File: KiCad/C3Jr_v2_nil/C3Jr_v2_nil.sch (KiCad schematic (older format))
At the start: 68 parts, among them IC1 ATTINY85-P, P1 PWM_0, P2 PWM_1, P3 A_IN, P4 ISP, P5 STACK-L, P6 STACK-R, P7 DC_IN_1, P8 DC_IN_2, Q1 PNP, Q2 PNP, X1 CRYSTAL

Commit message: C3Jr_v2_nil - Name in Lights for C3Jr - to light up custom names on face plates
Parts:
- added C3, C4, C5: 100n, symbol C
- C1, C2: value C -> 22p
- renumbered IC1 to U1
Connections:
- wire segments 202 -> 166
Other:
- moved on the sheet: P8

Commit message: C3Jr_v2_nil : Name in Lights, initial board layout.
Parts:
- removed D17, D18, D19, D20, D21, D22, D23, D24, D25, D26, D27, D28, D29, D30, D31, D32: LED, symbol LED
- removed P1: PWM_0, symbol CONN_2
- removed P2: PWM_1, symbol CONN_2
- removed Q2: PNP, symbol PNP
- removed R10: 1k, symbol R
- removed R11, R12, R13, R14, R15, R16, R17, R18: 47E, symbol R
- removed R20: 10k, symbol R
- removed R22: LDR2, symbol R
- removed X1: CRYSTAL, symbol CRYSTAL
- added CD2: CDOT2, symbol CONN_4
- added K1: CONN_3, symbol CONN_3
- added P10, P11, P14, P15, P9, rowBoB1: CONN_1, symbol CONN_1
- added P24, P25, P26, P27, P28, P29, P30, P31, P32, P33, P34, P35, P36, P37, P38, P39: DIL6, PROTO-6, symbol DIL6
- added SP1: SPEAKER, symbol CONN_2
- added X1: CRYSTAL2, symbol CRYSTAL2
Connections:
- net labels removed: MISO_PWM_1
- wire segments 166 -> 256
- no-connect marks 0 -> 6
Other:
- note added: "Mounting Holes"
- note added: "PROTO AREA"
- note added: "allows same board to be used\nat different locations by selecting\none of two PWM pins"
- note removed: "Enable/Disable\njumpers, if reqd.\nduring programming"
- note removed: "LOWER bank of LEDs"
- moved on the sheet: R1

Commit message: C3Jr_v2_nil - revised PCB , smaller size
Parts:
- removed P11, P14, P15, rowBoB1: CONN_1, symbol CONN_1
- removed P24, P25, P26, P27, P28, P29, P30, P31, P32, P33, P34, P35: DIL6, PROTO-6, symbol DIL6
- removed P5: STACK-L, symbol CONN_4
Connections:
- wire segments 256 -> 160
- no-connect marks 6 -> 2

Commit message: C3Jr_v2_nil - revised PCB , smaller size, removed ATTiny and other parts
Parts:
- removed C1, C2: 22p, symbol C
- removed C3, C4: 100n, symbol C
- removed CD2: CDOT2, symbol CONN_4
- removed P3: A_IN, symbol CONN_4
- removed P39: DIL6, PROTO-6, symbol DIL6
- removed P4: ISP, symbol CONN_6
- removed P6: STACK-R, symbol CONN_4
- removed P8: DC_IN_2, symbol CONN_2
- removed R19: 10k, symbol R
- removed R21: LDR1, symbol R
- removed U1: ATTINY85-P, DIP8, symbol ATTINY85-P
- removed X1: CRYSTAL2, symbol CRYSTAL2
- added P3, P4: CONN_1, symbol CONN_1
- P6: renamed from K1; value CONN_3 -> DC_IN_2
- Q1: value PNP -> PBSS9110Z
- renumbered P9 to P1, P10 to P2, P7 to P5, P36 to P7, P37 to P8, P38 to P9, R2 to R1, R3 to R2, R4 to R3, R5 to R4, R6 to R5, R7 to R6, R8 to R7, R9 to R8, R1 to R9
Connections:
- net labels removed: MISO_PWM1, MOSI_PWM0_SDA, PB3_ADC3, PB4_ADC2, RST, SCK_SCL
- wire segments 160 -> 83
- no-connect marks 2 -> 4
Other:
- note removed: "allows same board to be used\nat different locations by selecting\none of two PWM pins"
- note removed: "these are also used to\nmount the lower board\nto C3Jr @ Stack-LR"
- note removed: "to connect external\nanalog IN like LDR"
- moved on the sheet: C5, D1, D10, D11, D12, D13, D14, D15, D16, D2, D3, D4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

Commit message: C3Jr_v2_nil - work in progress on NiL board
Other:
- note added: "C3Jr-Name-in-Lights\n------------------------\nan array of 16 SMD LEDs driven either via Speaker Transistor on C3Jr\nusing SP1 for control signal and P5/P6 for Power (+5V, GND)\nOR, by using on board Transistor with Base Resistor, via any other\navailable control pin on the controller.\nIf using on-board Transistor, Pin 3 of connector P6 gets terminated\non Proto Area, and can be red-wired to app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"
- note removed: "UPPER bank of LEDs"
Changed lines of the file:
@@
-EESchema Schematic File Version 2  date 5/4/2012 5:25:38 PM
+EESchema Schematic File Version 2  date 5/5/2012 12:21:39 PM
 LIBS:C3Jr_v2_nil
 LIBS:ATtiny85_bmp
@@
 Sheet 1 1
 Title ""
-Date "4 may 2012"
+Date "5 may 2012"
 Rev ""
 Comp ""
@@
 Comment4 ""
 $EndDescr
+Text Notes 7050 6300 0    60   ~ 12
+C3Jr-Name-in-Lights\n------------------------\nan array of 16 SMD LEDs driven either via Speaker Transistor on C3Jr\nusing SP1 for control signal and P5/P6 for Power (+5V, GND)\nOR, by using on board Transistor with Base Resistor, via any other\navailable control pin on the controller.\nIf using on-board Transistor, Pin 3 of connector P6 gets terminated\non Proto Area, and can be red-wired to appropriate control pin.
 $Comp
 L CONN_1 P3
@@
 	1    0    0    -1
 $EndComp
-Text Notes 7250 3700 0    40   ~ 0
-UPPER bank of LEDs
 Text Notes 1350 3300 0    40   ~ 0
 these are also used to\nmount the Upper board\nto C3Jr @ Proto area

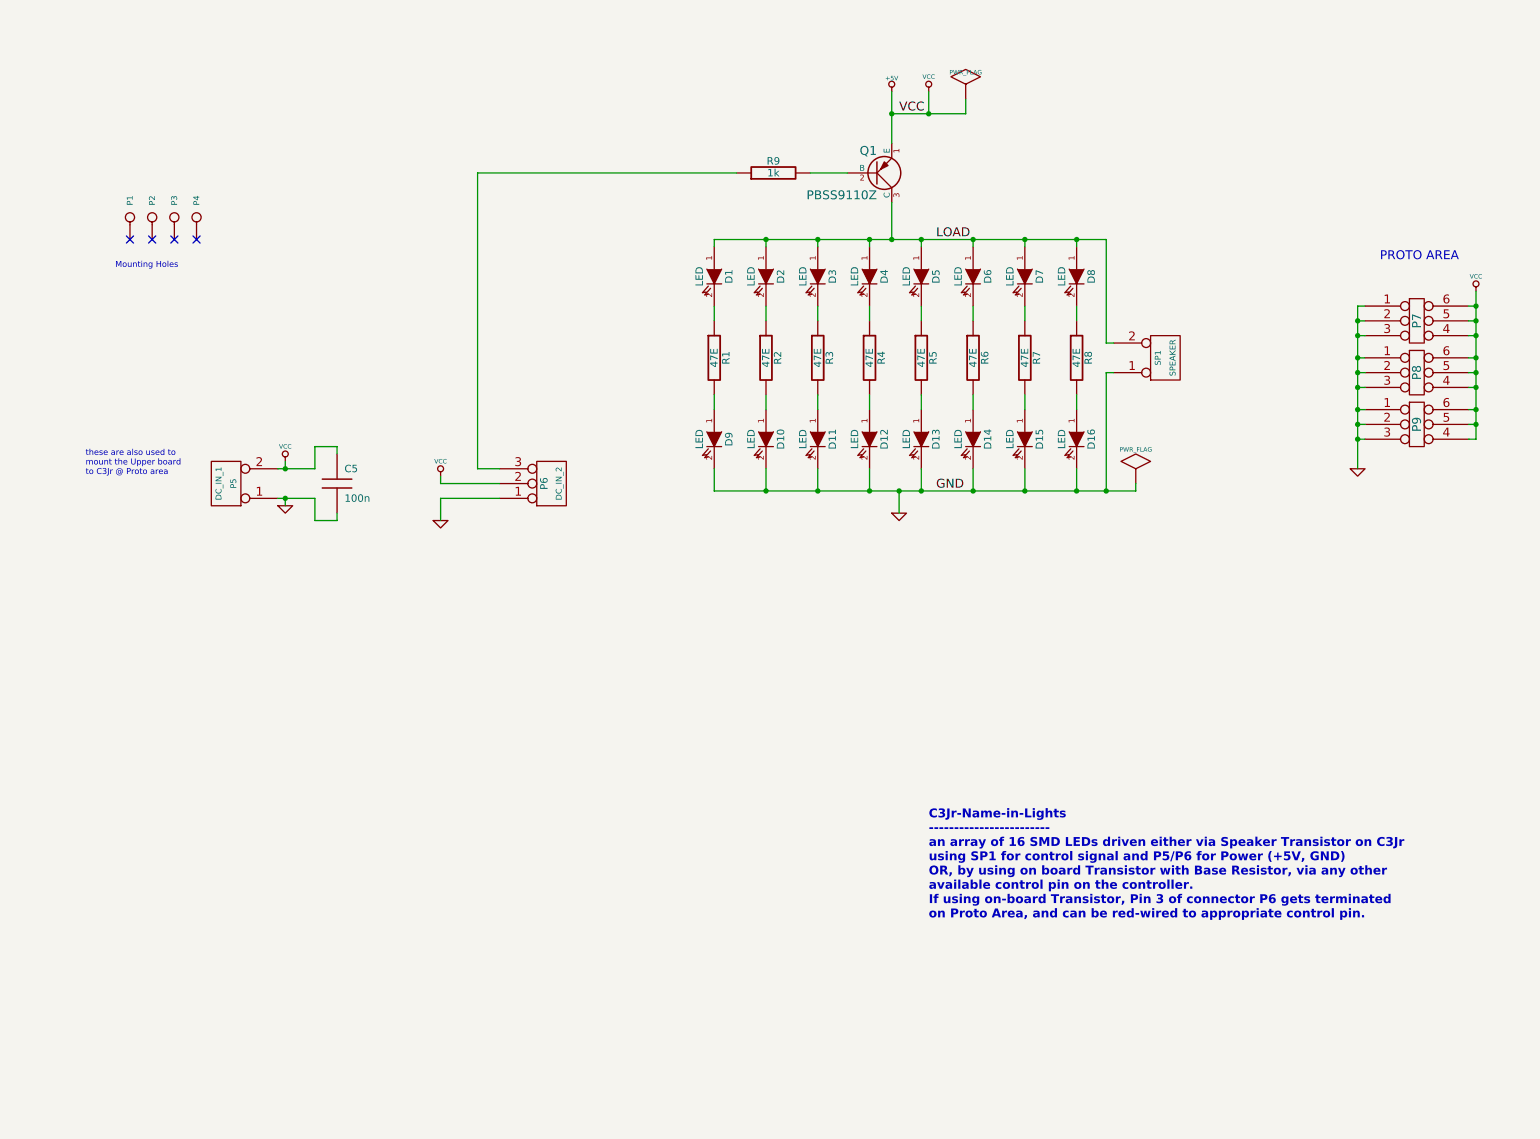
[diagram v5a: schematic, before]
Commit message: C3Jr_v2_nil : almost complete. Final checks required. Test circuit.
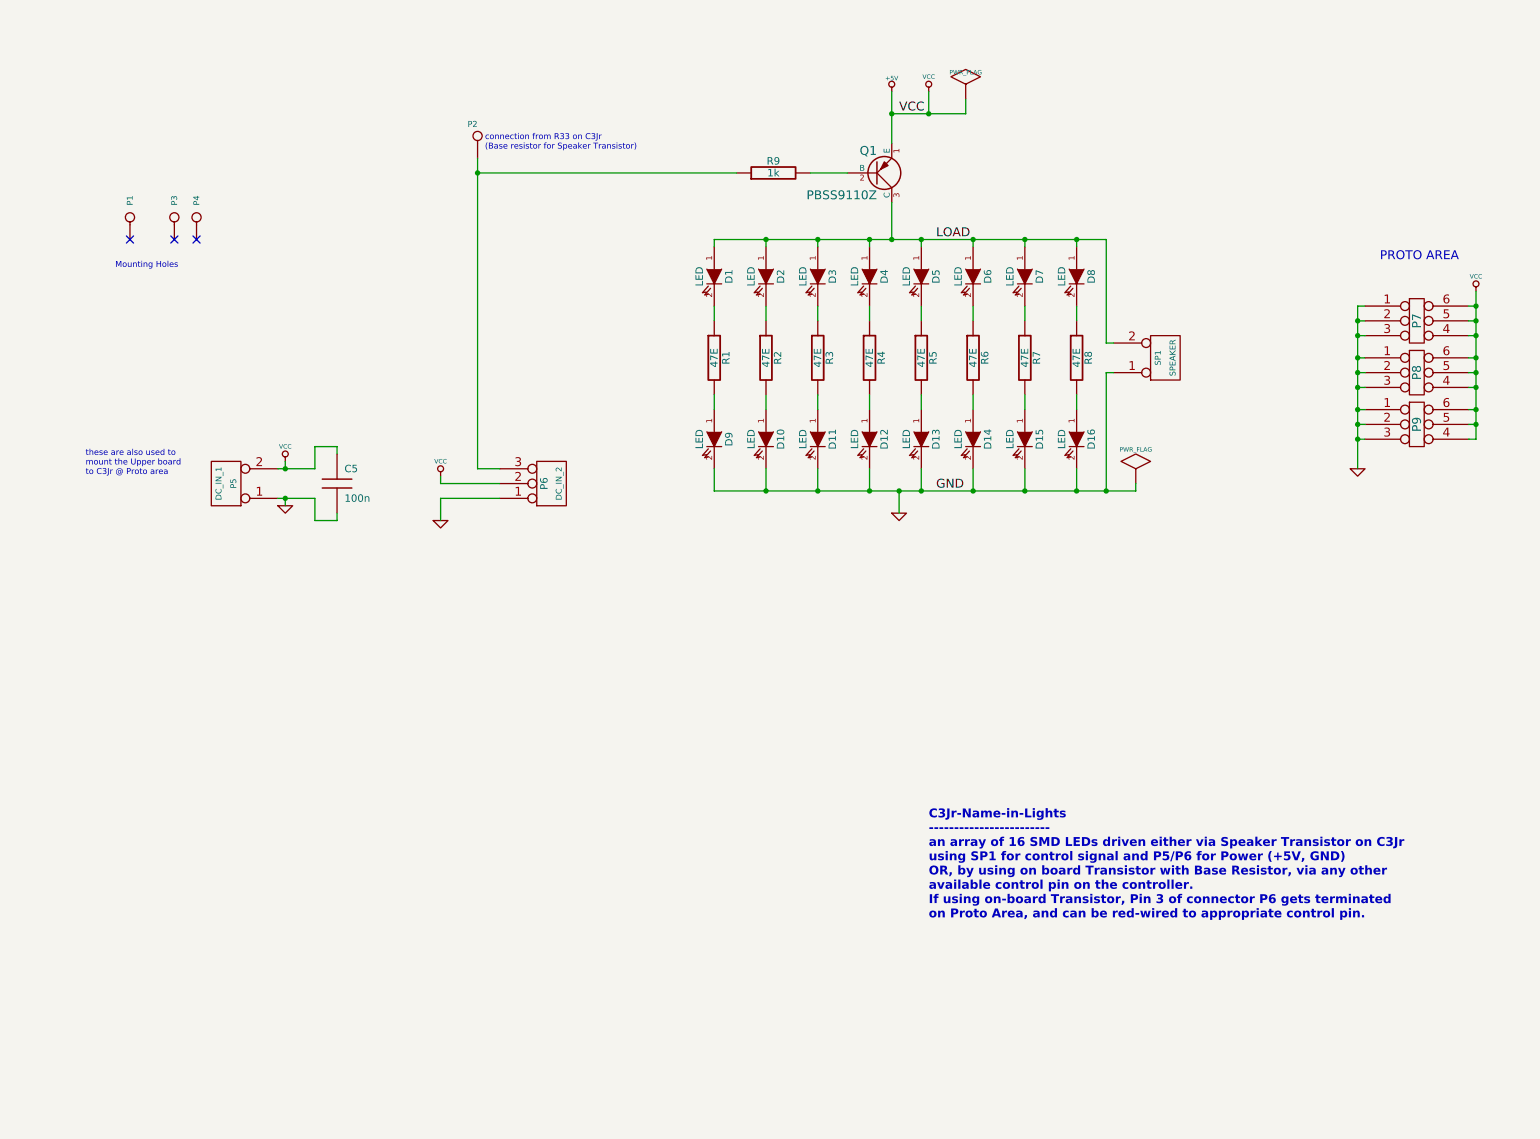
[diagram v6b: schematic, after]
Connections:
- net at P6.3 (P3), R9.1: now also P2.1
- no-connect marks 4 -> 3
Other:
- note added: "connection from R33 on C3Jr\n(Base resistor for Speaker Transistor)"
- moved on the sheet: P2
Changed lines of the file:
@@
-EESchema Schematic File Version 2  date 5/5/2012 12:21:39 PM
+EESchema Schematic File Version 2  date Sunday 06 May 2012 12:23:57 AM IST
 LIBS:C3Jr_v2_nil
 LIBS:ATtiny85_bmp
@@
 Comment4 ""
 $EndDescr
+Text Notes 4050 1100 0    40   ~ 0
+connection from R33 on C3Jr\n(Base resistor for Speaker Transistor)
+Connection ~ 4000 1250
+Wire Wire Line
+	4000 1150 4000 3250
+Wire Wire Line
+	9950 3250 9950 2150
+Connection ~ 8050 1700
+Wire Wire Line
+	8250 1700 5600 1700
+Wire Wire Line
+	8250 1700 8250 2400
+Wire Wire Line
+	8250 2400 8300 2400
+Connection ~ 2700 3450
+Wire Wire Line
+	2650 3450 2900 3450
+Wire Wire Line
+	2900 3450 2900 3600
+Wire Wire Line
+	2900 3600 3050 3600
+Wire Wire Line
+	3050 3600 3050 3550
+Wire Wire Line
+	4150 3350 3750 3350
+Wire Wire Line
+	3750 3350 3750 3300
+Wire Wire Line
+	2700 3500 2700 3450
+Wire Wire Line
+	2700 3200 2700 3250
+Wire Wire Line
+	7700 2150 7700 2250
+Wire Wire Line
+	7000 2150 7000 2250
+Wire Wire Line
+	6300 2150 6300 2250
+Wire Wire Line
+	5600 2150 5600 2250
+Connection ~ 6850 3400
+Wire Wire Line
+	6850 3400 6850 3550
+Wire Wire Line
+	6250 1250 6500 1250
+Wire Wire Line
+	6800 1050 6800 700
+Wire Wire Line
+	7700 1700 7700 1750
+Wire Wire Line
+	7000 1700 7000 1750
+Wire Wire Line
+	6300 1700 6300 1750
+Wire Wire Line
+	5600 1700 5600 1750
+Wire Wire Line
+	7700 2750 7700 2850
+Wire Wire Line
+	7000 2750 7000 2850
+Wire Wire Line
+	6300 2750 6300 2850
+Wire Wire Line
+	5600 2750 5600 2850
+Connection ~ 7350 3400
+Wire Wire Line
+	7350 3400 7350 3250
+Connection ~ 6650 3400
+Wire Wire Line
+	6650 3400 6650 3250
+Connection ~ 5950 3400
+Wire Wire Line
+	5950 3400 5950 3250
+Connection ~ 7350 1700
+Connection ~ 6650 1700
+Connection ~ 5950 1700
+Wire Wire Line
+	8050 3250 8050 3400
+Wire Wire Line
+	5600 3250 5600 3400
+Connection ~ 6300 1700
+Connection ~ 7000 1700
+Connection ~ 7700 1700
+Wire Wire Line
+	6300 3400 6300 3250
+Connection ~ 6300 3400
+Wire Wire Line
+	7000 3400 7000 3250
+Connection ~ 7000 3400
+Wire Wire Line
+	7700 3400 7700 3250
+Connection ~ 7700 3400
+Wire Wire Line
+	5950 2750 5950 2850
+Wire Wire Line
+	6650 2750 6650 2850
+Wire Wire Line
+	7350 2750 7350 2850
+Wire Wire Line
+	8050 2750 8050 2850
+Wire Wire Line
+	5950 1750 5950 1700
+Wire Wire Line
+	6650 1700 6650 1750
+Wire Wire Line
+	7350 1700 7350 1750
+Wire Wire Line
+	8050 1700 8050 1750
+Wire Wire Line
+	6800 1700 6800 1450
+Connection ~ 6800 1700
+Wire Wire Line
+	7050 700  7050 850
+Connection ~ 6800 850
+Wire Wire Line
+	7300 750  7300 850
+Wire Wire Line
+	7300 850  6800 850
+Connection ~ 7050 850
+Wire Wire Line
+	5950 2150 5950 2250
+Wire Wire Line
+	6650 2150 6650 2250
+Wire Wire Line
+	7350 2150 7350 2250
+Wire Wire Line
+	8050 2150 8050 2250
+Wire Wire Line
+	3750 3600 3750 3450
+Wire Wire Line
+	3750 3450 4150 3450
+Wire Wire Line
+	3050 3150 3050 3100
+Wire Wire Line
+	3050 3100 2900 3100
+Wire Wire Line
+	2900 3100 2900 3250
+Wire Wire Line
+	2900 3250 2650 3250
+Connection ~ 2700 3250
+Connection ~ 10750 2150
+Wire Wire Line
+	10750 2050 10750 3050
+Wire Wire Line
+	10750 3050 10700 3050
+Connection ~ 10750 2850
+Wire Wire Line
+	10750 2850 10700 2850
+Connection ~ 10750 2600
+Wire Wire Line
+	10750 2600 10700 2600
+Connection ~ 10750 2350
+Wire Wire Line
+	10750 2350 10700 2350
+Connection ~ 9950 2250
+Wire Wire Line
+	10000 2250 9950 2250
+Connection ~ 9950 2500
+Wire Wire Line
+	9950 2500 10000 2500
+Connection ~ 9950 2700
+Wire Wire Line
+	9950 2700 10000 2700
+Connection ~ 9950 2950
+Wire Wire Line
+	9950 2950 10000 2950
+Wire Wire Line
+	10750 2150 10700 2150
+Wire Wire Line
+	9950 2150 10000 2150
+Wire Wire Line
+	9950 3050 10000 3050
+Connection ~ 9950 3050
+Wire Wire Line
+	9950 2850 10000 2850
+Connection ~ 9950 2850
+Wire Wire Line
+	9950 2600 10000 2600
+Connection ~ 9950 2600
+Wire Wire Line
+	9950 2350 10000 2350
+Connection ~ 9950 2350
+Wire Wire Line
+	10750 2250 10700 2250
+Connection ~ 10750 2250
+Wire Wire Line
+	10750 2500 10700 2500
+Connection ~ 10750 2500
+Wire Wire Line
+	10750 2700 10700 2700
+Connection ~ 10750 2700
+Wire Wire Line
+	10750 2950 10700 2950
+Connection ~ 10750 2950
+Wire Wire Line
+	8300 2600 8250 2600
+Wire Wire Line
+	8250 2600 8250 3400
+Connection ~ 8050 3400
+Wire Wire Line
+	4000 1250 5750 1250
+Wire Wire Line
+	4000 3250 4150 3250
+Wire Wire Line
+	8450 3350 8450 3400
+Wire Wire Line
+	8450 3400 5600 3400
+Connection ~ 8250 3400
 Text Notes 7050 6300 0    60   ~ 12
 C3Jr-Name-in-Lights\n------------------------\nan array of 16 SMD LEDs driven either via Speaker Transistor on C3Jr\nusing SP1 for control signal and P5/P6 for Power (+5V, GND)\nOR, by using on board Transistor with Base Resistor, via any other\navailable control pin on the controller.\nIf using on-board Transistor, Pin 3 of connector P6 gets terminated\non Proto Area, and can be red-wired to appropriate control pin.
@@
 $EndComp
 NoConn ~ 2100 1700
-Connection ~ 8250 3400
-Wire Wire Line
-	8450 3400 5600 3400
-Wire Wire Line
-	8450 3400 8450 3350
-Wire Wire Line
-	4150 3250 4000 3250
-Wire Wire Line
-	4000 3250 4000 1250
-Wire Wire Line
-	4000 1250 5750 1250
-Connection ~ 8050 3400
-Wire Wire Line
-	8250 3400 8250 2600
-Wire Wire Line
-	8250 2600 8300 2600
-Connection ~ 10750 2950
-Wire Wire Line
-	10750 2950 10700 2950
-Connection ~ 10750 2700
-Wire Wire Line
-	10750 2700 10700 2700
-Connection ~ 10750 2500
-Wire Wire Line
-	10750 2500 10700 2500
-Connection ~ 10750 2250
-Wire Wire Line
-	10750 2250 10700 2250
-Connection ~ 9950 2350
-Wire Wire Line
-	9950 2350 10000 2350
-Connection ~ 9950 2600
-Wire Wire Line
-	9950 2600 10000 2600
-Connection ~ 9950 2850
-Wire Wire Line
-	9950 2850 10000 2850
-Connection ~ 9950 3050
-Wire Wire Line
-	9950 3050 10000 3050
-Wire Wire Line
-	10000 2150 9950 2150
-Wire Wire Line
-	10750 2150 10700 2150
-Wire Wire Line
-	9950 2950 10000 2950
-Connection ~ 9950 2950
-Wire Wire Line
-	9950 2700 10000 2700
-Connection ~ 9950 2700
-Wire Wire Line
-	9950 2500 10000 2500
-Connection ~ 9950 2500
-Wire Wire Line
-	10000 2250 9950 2250
-Connection ~ 9950 2250
-Wire Wire Line
-	10750 2350 10700 2350
-Connection ~ 10750 2350
-Wire Wire Line
-	10750 2600 10700 2600
-Connection ~ 10750 2600
-Wire Wire Line
-	10750 2850 10700 2850
-Connection ~ 10750 2850
-Wire Wire Line
-	10700 3050 10750 3050
-Wire Wire Line
-	10750 3050 10750 2050
-Connection ~ 10750 2150
-Connection ~ 2700 3250
-Wire Wire Line
-	2650 3250 2900 3250
-Wire Wire Line
-	2900 3250 2900 3100
-Wire Wire Line
-	2900 3100 3050 3100
-Wire Wire Line
-	3050 3100 3050 3150
-Wire Wire Line
-	4150 3450 3750 3450
-Wire Wire Line
-	3750 3450 3750 3600
-Wire Wire Line
-	8050 2150 8050 2250
-Wire Wire Line
-	7350 2150 7350 2250
-Wire Wire Line
-	6650 2150 6650 2250
-Wire Wire Line
-	5950 2150 5950 2250
-Connection ~ 7050 850
-Wire Wire Line
-	6800 850  7300 850
-Wire Wire Line
-	7300 850  7300 750
-Connection ~ 6800 850
-Wire Wire Line
-	7050 700  7050 850
-Connection ~ 6800 1700
-Wire Wire Line
-	6800 1700 6800 1450
-Wire Wire Line
-	8050 1700 8050 1750
-Wire Wire Line
-	7350 1700 7350 1750
-Wire Wire Line
-	6650 1700 6650 1750
-Wire Wire Line
-	5950 1750 5950 1700
-Wire Wire Line
-	8050 2750 8050 2850
-Wire Wire Line
-	7350 2750 7350 2850
-Wire Wire Line
-	6650 2750 6650 2850
-Wire Wire Line
-	5950 2750 5950 2850
-Connection ~ 7700 3400
-Wire Wire Line
-	7700 3400 7700 3250
-Connection ~ 7000 3400
-Wire Wire Line
-	7000 3400 7000 3250
-Connection ~ 6300 3400
-Wire Wire Line
-	6300 3400 6300 3250
-Connection ~ 7700 1700
-Connection ~ 7000 1700
-Connection ~ 6300 1700
-Wire Wire Line
-	5600 3400 5600 3250
-Wire Wire Line
-	8050 3250 8050 3400
-Connection ~ 5950 1700
-Connection ~ 6650 1700
-Connection ~ 7350 1700
-Wire Wire Line
-	5950 3400 5950 3250
-Connection ~ 5950 3400
-Wire Wire Line
-	6650 3400 6650 3250
-Connection ~ 6650 3400
-Wire Wire Line
-	7350 3400 7350 3250
-Connection ~ 7350 3400
-Wire Wire Line
-	5600 2750 5600 2850
-Wire Wire Line
-	6300 2750 6300 2850
-Wire Wire Line
-	7000 2750 7000 2850
-Wire Wire Line
-	7700 2750 7700 2850
-Wire Wire Line
-	5600 1750 5600 1700
-Wire Wire Line
-	6300 1700 6300 1750
-Wire Wire Line
-	7000 1700 7000 1750
-Wire Wire Line
-	7700 1700 7700 1750
-Wire Wire Line
-	6800 1050 6800 700
-Wire Wire Line
-	6250 1250 6500 1250
-Wire Wire Line
-	6850 3400 6850 3550
-Connection ~ 6850 3400
-Wire Wire Line
-	5600 2150 5600 2250
-Wire Wire Line
-	6300 2150 6300 2250
-Wire Wire Line
-	7000 2150 7000 2250
-Wire Wire Line
-	7700 2150 7700 2250
-Wire Wire Line
-	2700 3200 2700 3250
-Wire Wire Line
-	2700 3500 2700 3450
-Wire Wire Line
-	3750 3300 3750 3350
-Wire Wire Line
-	3750 3350 4150 3350
-Wire Wire Line
-	3050 3550 3050 3600
-Wire Wire Line
-	3050 3600 2900 3600
-Wire Wire Line
-	2900 3600 2900 3450
-Wire Wire Line
-	2900 3450 2650 3450
-Connection ~ 2700 3450
-Wire Wire Line
-	8300 2400 8250 2400
-Wire Wire Line
-	8250 2400 8250 1700
-Wire Wire Line
-	8250 1700 5600 1700
-Connection ~ 8050 1700
-Wire Wire Line
-	9950 2150 9950 3250
 $Comp
 L PWR_FLAG #FLG01
@@
 	1    0    0    1
 $EndComp
-NoConn ~ 1800 1700
 $Comp
 L CONN_1 P2
 U 1 1 4F9EEE67
-P 1800 1550
-F 0 "P2" H 1880 1550 40  0000 L CNN
-F 1 "CONN_1" H 1800 1605 30  0001 C CNN
-	1    1800 1550
+P 4000 1000
+F 0 "P2" V 4080 1000 40  0000 L CNN
+F 1 "CONN_1" H 4000 1055 30  0001 C CNN
+	1    4000 1000
 	0    -1   -1   0
 $EndComp
